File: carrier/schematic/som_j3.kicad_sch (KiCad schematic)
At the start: 1 part, among them J26003 DF40C-100DS-0.4V(51)

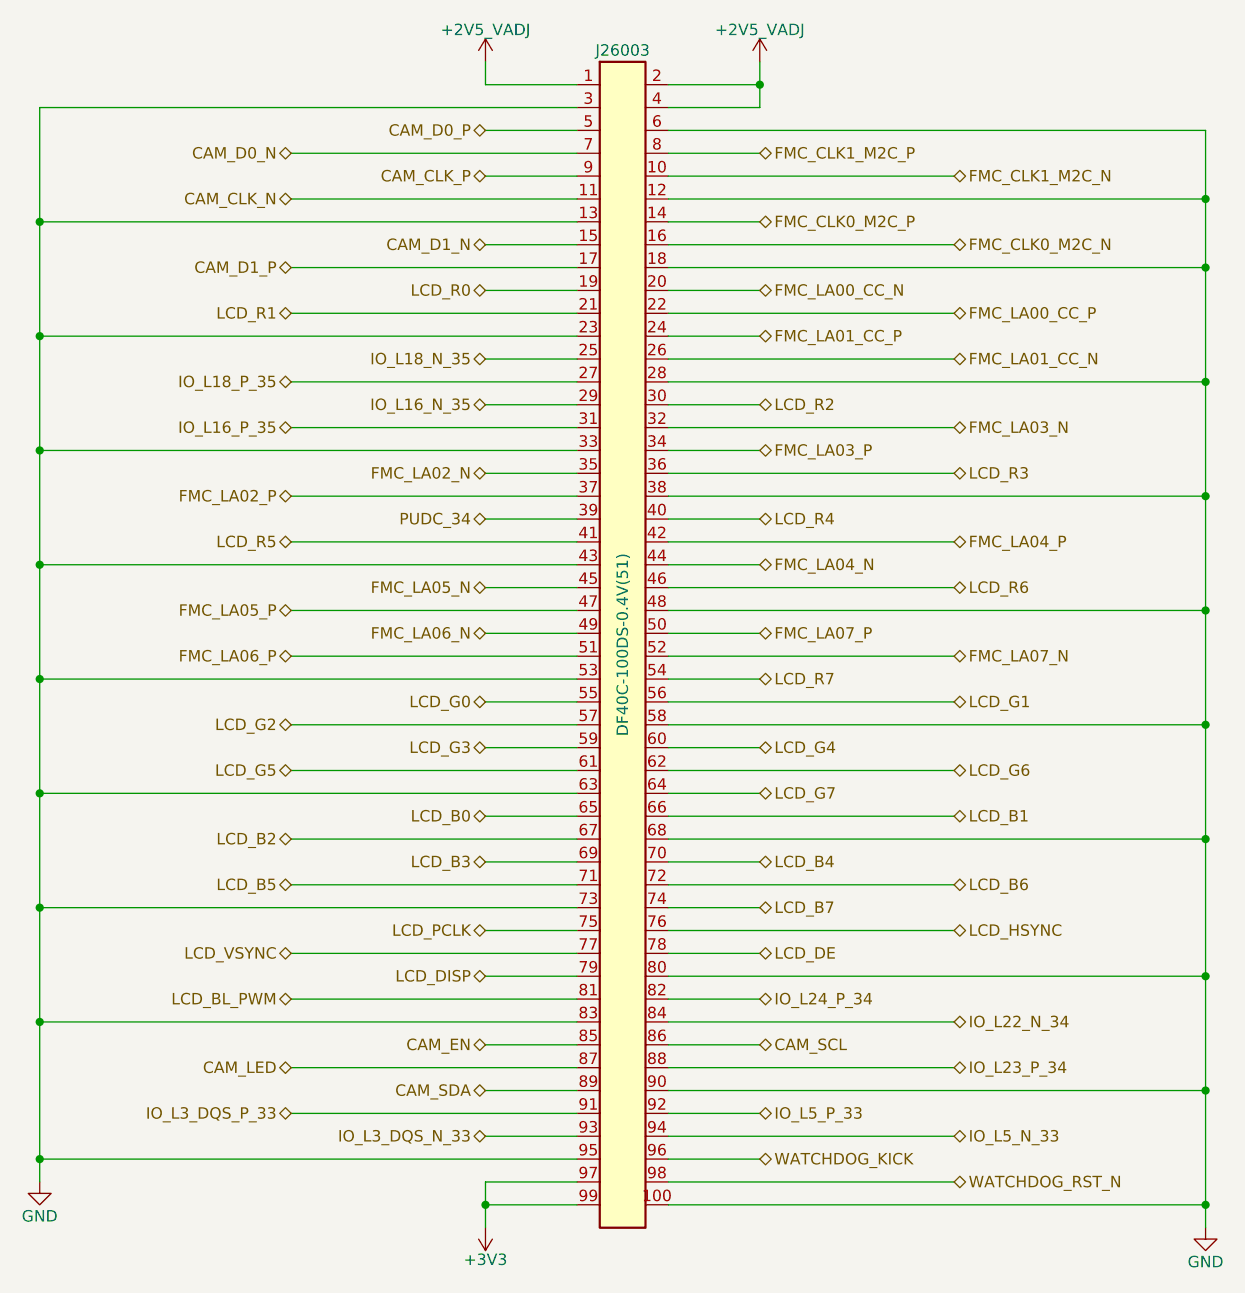
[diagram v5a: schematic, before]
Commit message: fix(coord CRITICAL CLOSED): DF40 no-mate — carrier J1/J2/J3 DS receptacle -> DP plug
SOM<->carrier coordination audit found the assembled stack physically CANNOT MATE:
both the SOM (fabricated DS land/BOM) and the carrier instantiated the DF40C-100DS
RECEPTACLE (C597931). DF40 mates only DP-plug <-> DS-receptacle, so two receptacles
= zero connection on all 300 pins. Independently re-verified 3/3 (the carrier
som_j1/2/3 really used DS; the geometry/mating confirmed from the footprints).

Fix (carrier = schgen-controlled side carries the plug): som_conn_gen instantiates
DF40C-100DP-0.4V(51) = LCSC C531031 (verified via the LCSC/EasyEDA API + part-add,
faithful footprint + 3D). The DP pads 1-100 keep the SAME contract net->pad-number
map; the Hirose DP/DS pair mates pad-N<->pad-N by design (the DP's mirrored pin-1
X=-9.8 vs DS X=+9.8 IS the face-to-face mating geometry, and the ±1.355 plug rows
nest in the ±1.60 receptacle rows). The DP's 4 mechanical hold-down pads (101-104)
are NC. The SOM stays DS (its fabricated land/BOM) -> the pair now mates.

Verified: 154x137, DRC 0, BOARD PASS, 3D 57/57, RATSNEST/PLACEMENT/CONNECTOR-MODEL
/SPACING all PASS, golden blessed; 39 som_j tests pass (DS->DP, 104-pad, 101-104 NC).

Co-Authored-By: Claude Opus 4.8 <noreply@anthropic.com>
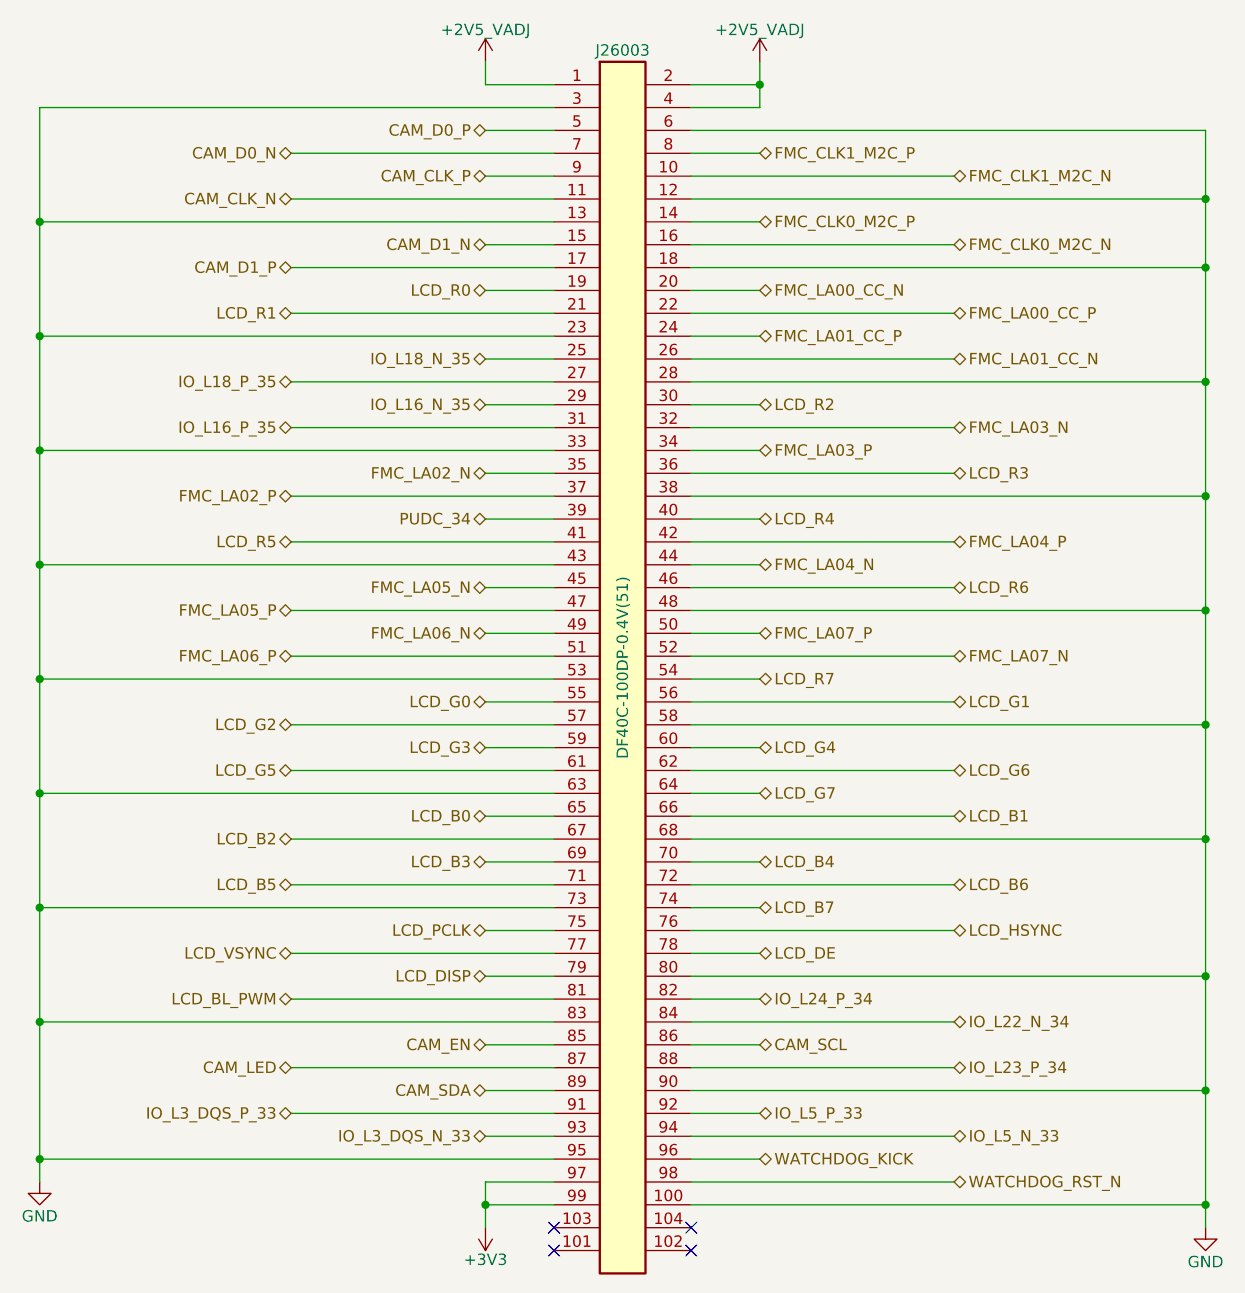
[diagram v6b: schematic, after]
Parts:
- J26003: value DF40C-100DS-0.4V(51) -> DF40C-100DP-0.4V(51); footprint DF40C-100DS-0.4V_51:DF40C-100DS-0.4V_51 -> DF40C-100DP-0.4V_51:DF40C-100DP-0.4V_51; symbol DF40C-100DS-0.4V_51:DF40C-100DS-0.4V_51 -> DF40C-100DP-0.4V_51:DF40C-100DP-0.4V_51; LCSC C597931 -> C531031
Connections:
- no-connect marks 0 -> 4

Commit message: feat(motor_io): generic 8-ch PWM/ESC out + motor-rail telemetry (drone demo)
A reusable benchtop drone-capability interface, split into two carrier-local
subsystems so neither defeats the per-sheet placer:
 * motor_pwm  — 8 PWM/ESC outputs: Zynq PL (8 free bank-33 LVCMOS33 pins) ->
   SN74HCT245 octal buffer (3.3->5V, ISOLATES the PL) -> 3x8 servo header J1.
   #OE 10k pull-up = outputs HiZ until the PL arms (fail-safe). SY6280 (U3)
   current-limits the header's +5V servo row (a servo short can't crash +5V).
 * motor_sense — in-line motor-rail telemetry: battery passes J2(XT60 in) -> RS1
   10mR shunt -> J3(XT60 out) -> off-board ESCs; INA3221 (0x42) reads current
   AND bus-V on one channel; SMBJ28A TVS; CRITICAL -> ESC_FAULT_N PL alert.

All sensors stay OFF-BOARD on the existing PMOD/QWIIC/J11001 headers (no new
sensor connectors); vision is the existing camera FFC + PL fabric. The 10
IO->ESC FUNCTION_MAP renames use contract pins RE-VERIFIED free (XDC 'unclaimed',
no consumer, no double-claim — LAW 0); the XDC regenerates them.

Two placer engine fixes (improve the algorithm, never bend a part):
 * _trunk_series_columns — a 2-pin shunt bridging two SIGNAL trunks (RS1) had no
   template; drawn as a labelled column. Guarded (s[0] not in _done) so every
   existing sheet stays byte-identical.
 * cross-edge corner-overlap rejection in floorplan._attempt_pack — the per-edge
   1D packer let a W-edge and an S-edge block overlap at the corner (the
   motor_sense XT60 shorted HDMI_RX_5V); now the grow loop sizes the board until
   clear. No-op on clean boards (verified, closest gap 34x CLEAR).

Phase-3 adversarial review (10 agents) corrections landed: buffer-levels / SY6280
/ PL-pins / INA-wiring / passives all verified CLEAN; fixed the 33R doc-vs-netlist
contradiction + added the rail CURRENT bound (<=7A, the 1W shunt limit) next to
the <=4S voltage bound. Tracked (NOT abandoned) to instantiate: 33R series-damping
(sourced C25508 but the 2-array form trips the place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
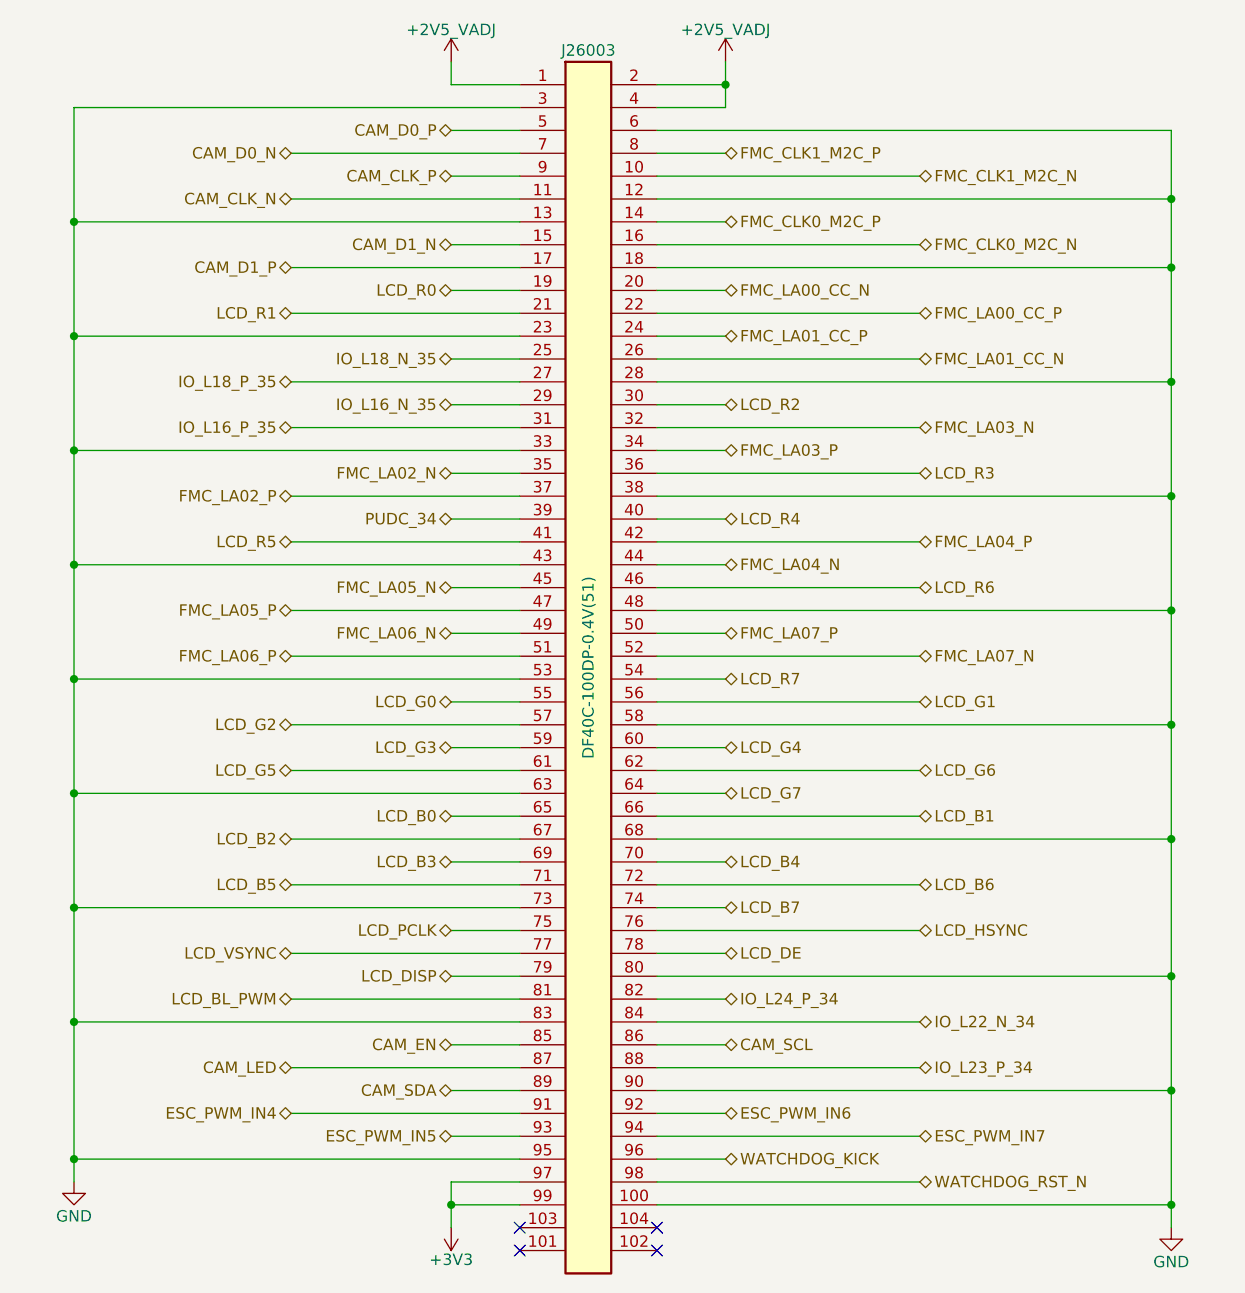
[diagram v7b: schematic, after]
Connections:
- net IO_L3_DQS_N_33 renamed ESC_PWM_IN5
- net IO_L3_DQS_P_33 renamed ESC_PWM_IN4
- net IO_L5_N_33 renamed ESC_PWM_IN7
- net IO_L5_P_33 renamed ESC_PWM_IN6
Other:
- moved on the sheet: J26003
